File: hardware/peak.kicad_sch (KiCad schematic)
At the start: 29 parts, among them J1 Conn_Controller, J2 Conn_Buttons, J3 Conn_CAN, J4 Conn_Display, J5 Conn_DEBUG, Q1 AO3400A, U1 ESP32-S3-WROOM-1, U2 TLV76733DRVx, U3 MCP2542FDxMF

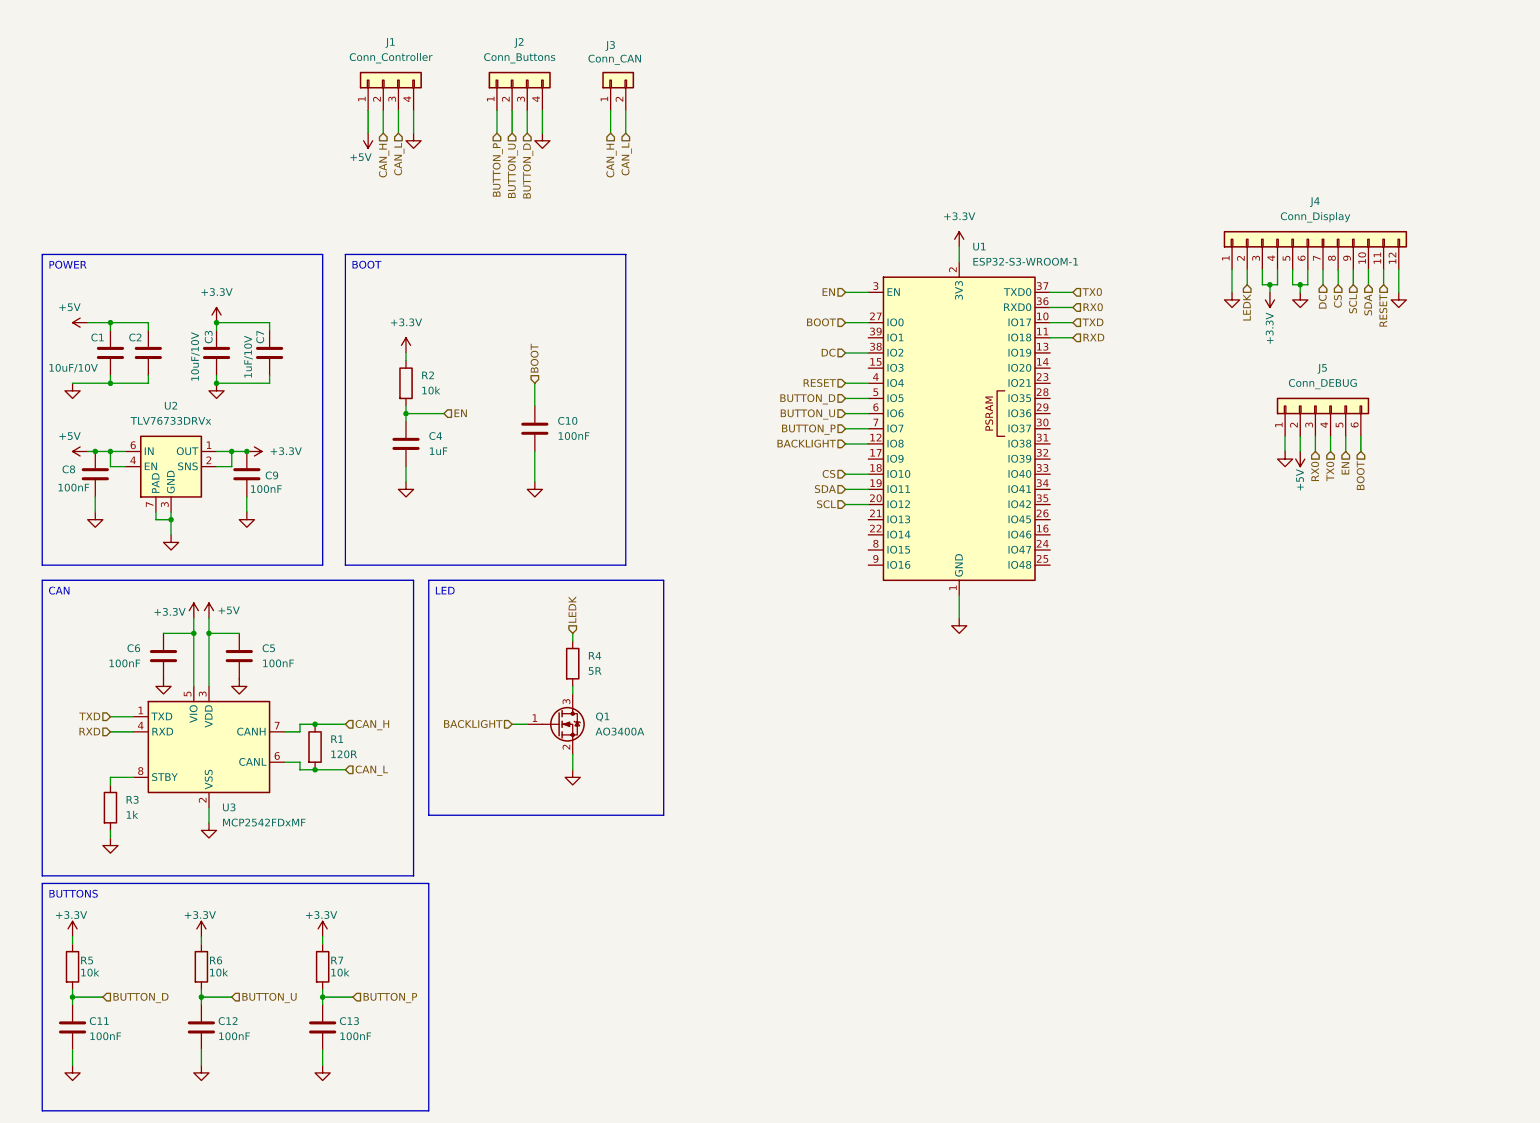
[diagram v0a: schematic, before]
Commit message: ✨ Add schematic parts
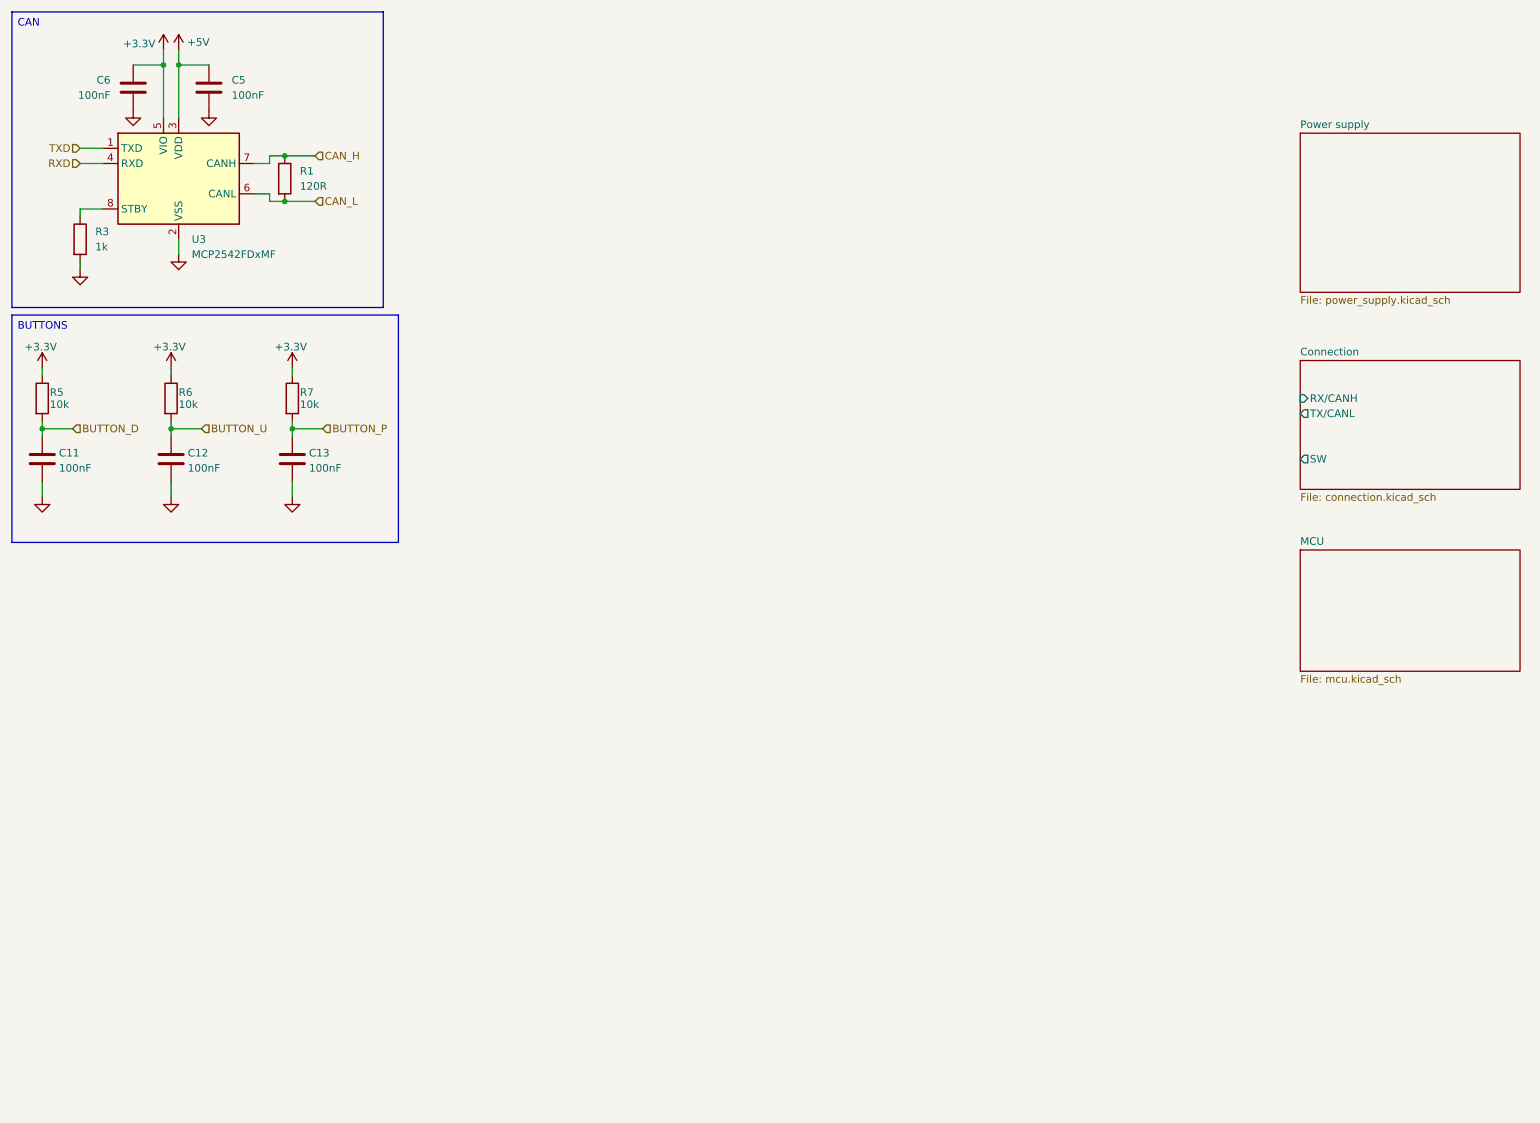
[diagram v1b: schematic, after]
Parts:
- removed C1, C2, C3: 10uF/10V, Capacitor_SMD:C_0805_2012Metric, symbol Device:C
- removed C10, C8, C9: 100nF, Capacitor_SMD:C_0603_1608Metric, symbol Device:C
- removed C4: 1uF, Capacitor_SMD:C_0603_1608Metric, symbol Device:C
- removed C7: 1uF/10V, Capacitor_SMD:C_0805_2012Metric, symbol Device:C
- removed J1: Conn_Controller, Connector_Molex:Molex_PicoBlade_53261-0471_1x04-1MP_P1.25mm_Horizontal, symbol Connector_Generic:Conn_01x04
- removed J2: Conn_Buttons, Connector_Molex:Molex_PicoBlade_53261-0471_1x04-1MP_P1.25mm_Horizontal, symbol Connector_Generic:Conn_01x04
- removed J3: Conn_CAN, Connector_Molex:Molex_PicoBlade_53261-0271_1x02-1MP_P1.25mm_Horizontal, symbol Connector_Generic:Conn_01x02
- removed J4: Conn_Display, lib:ST7789V2, symbol Connector_Generic:Conn_01x12
- removed J5: Conn_DEBUG, lib:DEBUG_SMD, symbol Connector_Generic:Conn_01x06
- removed Q1: AO3400A, PCM_Package_TO_SOT_SMD_AKL:SOT-23, symbol Transistor_FET:AO3400A
- removed R2: 10k, PCM_Resistor_SMD_AKL:R_0603_1608Metric, symbol Device:R
- removed R4: 5R, PCM_Resistor_SMD_AKL:R_0805_2012Metric, symbol Device:R
- removed U1: ESP32-S3-WROOM-1, RF_Module:ESP32-S3-WROOM-1, symbol RF_Module:ESP32-S3-WROOM-1
- removed U2: TLV76733DRVx, Package_SON:WSON-6-1EP_2x2mm_P0.65mm_EP1x1.6mm_ThermalVias, symbol Regulator_Linear:TLV76733DRVx
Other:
- added sheet Connection (connection.kicad_sch)
- added sheet MCU (mcu.kicad_sch)
- added sheet Power supply (power_supply.kicad_sch)
- moved on the sheet: C11, C12, C13, C5, C6, R1, R3, R5, R6, R7, U3

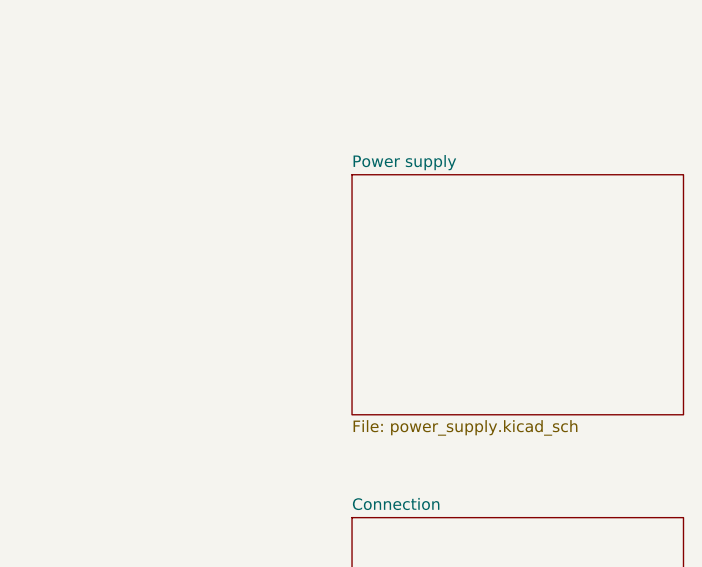
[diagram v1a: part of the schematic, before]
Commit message: ✨ Add pulldown to disable the led by default
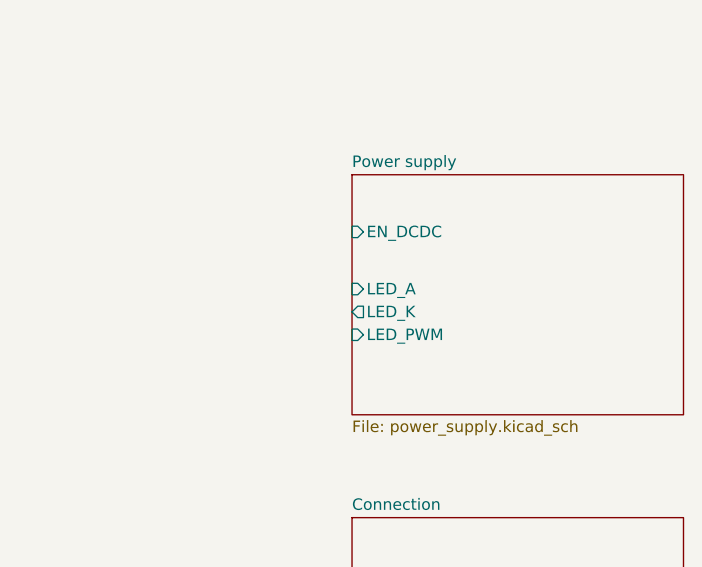
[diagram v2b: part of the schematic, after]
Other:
- sheet Power supply ports: added EN_DCDC, LED_A, LED_K, LED_PWM; removed none
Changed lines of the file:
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@@
+			)
+		)
+		(pin "EN_DCDC" input
+			(at 229.87 40.64 180)
+			(effects
+				(font
+					(size 1.27 1.27)
+				)
+				(justify left)
+			)
+		)
+		(pin "LED_A" input
+			(at 229.87 46.99 180)
+			(effects
+				(font
+					(size 1.27 1.27)
+				)
+				(justify left)
+			)
+		)
+		(pin "LED_K" output
+			(at 229.87 49.53 180)
+			(effects
+				(font
+					(size 1.27 1.27)
+				)
+				(justify left)
+			)
+		)
+		(pin "LED_PWM" input
+			(at 229.87 52.07 180)
+			(effects
+				(font
+					(size 1.27 1.27)
+				)
+				(justify left)
 			)
 		)

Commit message: ✨ Further schematic updates
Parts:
- removed C11, C12, C13, C5, C6: 100nF, Capacitor_SMD:C_0603_1608Metric, symbol Device:C
- removed R1: 120R, PCM_Resistor_SMD_AKL:R_0603_1608Metric, symbol Device:R
- removed R3: 1k, PCM_Resistor_SMD_AKL:R_0603_1608Metric, symbol Device:R
- removed R5, R6, R7: 10k, PCM_Resistor_SMD_AKL:R_0603_1608Metric, symbol Device:R
- removed U3: MCP2542FDxMF, Package_DFN_QFN:DFN-8-1EP_3x3mm_P0.65mm_EP1.55x2.4mm, symbol Interface_CAN_LIN:MCP2542FDxMF
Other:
- added sheet Display (display.kicad_sch)
- added sheet IO (io.kicad_sch)
- sheet MCU ports: added EN_DCDC, FB_DCDC; removed none
- sheet Power supply ports: added FB_DCDC; removed LED_A, LED_K, LED_PWM

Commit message: ✨ MCU updates
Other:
- added sheet Wireless (wireless.kicad_sch)
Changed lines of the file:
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@@
 	(wire
 		(pts
-			(xy 213.36 41.91) (xy 226.06 41.91)
+			(xy 173.99 59.69) (xy 226.06 59.69)
 		)
 		(stroke
@@
 	(wire
 		(pts
-			(xy 213.36 44.45) (xy 227.33 44.45)
+			(xy 173.99 62.23) (xy 227.33 62.23)
 		)
 		(stroke
@@
 	(wire
 		(pts
-			(xy 227.33 44.45) (xy 227.33 43.18)
-		)
-		(stroke
-			(width 0)
-			(type default)
-		)
-	)
-	(wire
-		(pts
-			(xy 226.06 41.91) (xy 226.06 40.64)
+			(xy 227.33 62.23) (xy 227.33 43.18)
+		)
+		(stroke
+			(width 0)
+			(type default)
+		)
+	)
+	(wire
+		(pts
+			(xy 226.06 59.69) (xy 226.06 40.64)
 		)
 		(stroke
@@
 	)
 	(sheet
-		(at 181.61 68.58)
+		(at 64.77 71.12)
 		(size 21.59 39.37)
 		(exclude_from_sim no)
@@
 		)
 		(property "Sheetname" "Display"
-			(at 181.61 67.8684 0)
+			(at 64.77 70.4084 0)
 			(effects
 				(font
@@
 		)
 		(property "Sheetfile" "display.kicad_sch"
-			(at 181.61 108.5346 0)
+			(at 64.77 111.0746 0)
 			(effects
 				(font
@@
 		)
 		(pin "DISPLAY_RESET" input
-			(at 203.2 74.93 0)
+			(at 86.36 77.47 0)
 			(effects
 				(font
@@
 		)
 		(pin "DISPLAY_TE" input
-			(at 203.2 77.47 0)
+			(at 86.36 80.01 0)
 			(effects
 				(font
@@
 		)
 		(pin "LED_PWM" input
-			(at 203.2 80.01 0)
+			(at 86.36 82.55 0)
 			(effects
 				(font
@@
 		)
 		(pin "MIPI_CLN" input
-			(at 203.2 82.55 0)
+			(at 86.36 85.09 0)
 			(effects
 				(font
@@
 		)
 		(pin "MIPI_CLP" input
-			(at 203.2 85.09 0)
+			(at 86.36 87.63 0)
 			(effects
 				(font
@@
 		)
 		(pin "MIPI_D0N" input
-			(at 203.2 87.63 0)
+			(at 86.36 90.17 0)
 			(effects
 				(font
@@
 		)
 		(pin "MIPI_D0P" input
-			(at 203.2 90.17 0)
+			(at 86.36 92.71 0)
 			(effects
 				(font
@@
 		)
 		(pin "MIPI_D1N" input
-			(at 203.2 92.71 0)
+			(at 86.36 95.25 0)
 			(effects
 				(font
@@
 		)
 		(pin "MIPI_D1P" input
-			(at 203.2 95.25 0)
+			(at 86.36 97.79 0)
 			(effects
 				(font
@@
 	)
 	(sheet
-		(at 176.53 36.83)
+		(at 125.73 104.14)
+		(size 33.02 31.75)
+		(exclude_from_sim no)
+		(in_bom yes)
+		(on_board yes)
+		(dnp no)
+		(fields_autoplaced yes)
+		(stroke
+			(width 0.1524)
+			(type solid)
+		)
+		(fill
+			(color 0 0 0 0.0000)
+		)
+		(property "Sheetname" "Wireless"
+			(at 125.73 103.4284 0)
+			(effects
+				(font
+					(size 1.27 1.27)
+				)
+				(justify left bottom)
+			)
+		)
+		(property "Sheetfile" "wireless.kicad_sch"
+			(at 125.73 136.4746 0)
+			(effects
+				(font
+					(size 1.27 1.27)
+				)
+				(justify left top)
+			)
+		)
+		(instances
+			(project "peak"
+				(path "/54a54a18-4a65-4728-b17a-32b4a97370c1"
+					(page "7")
+				)
+			)
+		)
+	)
+	(sheet
+		(at 137.16 54.61)
 		(size 36.83 20.32)
 		(exclude_from_sim no)
@@
 		)
 		(property "Sheetname" "MCU"
-			(at 176.53 36.1184 0)
+			(at 137.16 53.8984 0)
 			(effects
 				(font
@@
 		)
 		(property "Sheetfile" "mcu.kicad_sch"
-			(at 176.53 57.7346 0)
+			(at 137.16 75.5146 0)
 			(effects
 				(font
@@
 		)
 		(pin "EN_DCDC" input
-			(at 213.36 41.91 0)
+			(at 173.99 59.69 0)
 			(effects
 				(font
@@
 		)
 		(pin "FB_DCDC" input
-			(at 213.36 44.45 0)
-			(effects
-				(font
+			(at 173.99 62.23 0)
+			(effects
+				(font

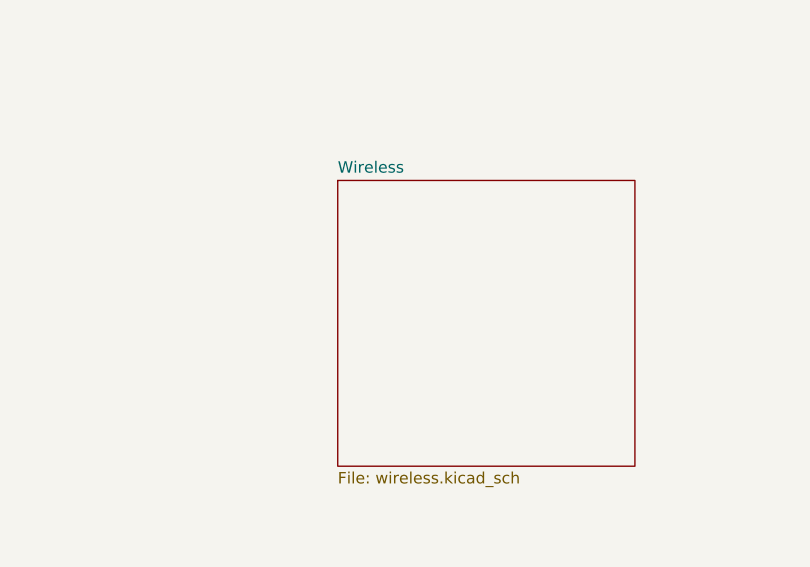
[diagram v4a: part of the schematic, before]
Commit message: ✨ Done wireless schematic
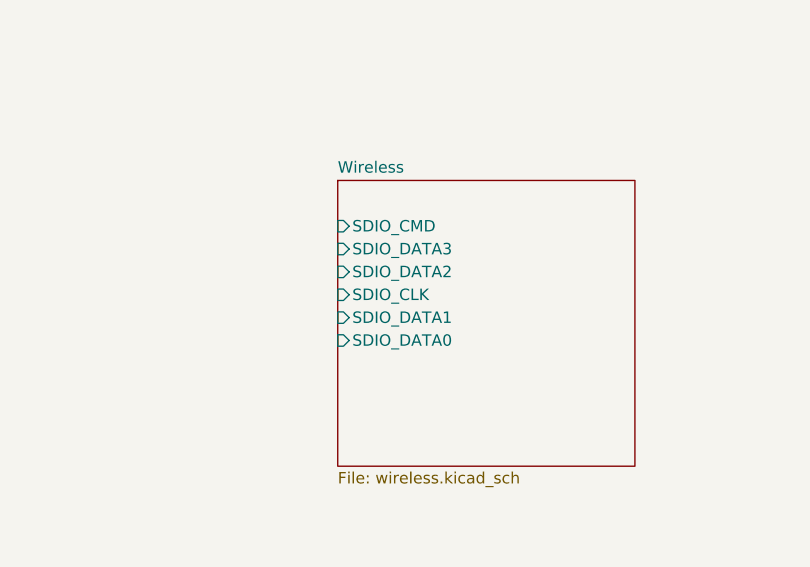
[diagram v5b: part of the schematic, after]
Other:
- sheet Wireless ports: added SDIO_CLK, SDIO_CMD, SDIO_DATA0, SDIO_DATA1, SDIO_DATA2, SDIO_DATA3; removed none
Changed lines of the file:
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@@
+			)
+		)
+		(pin "SDIO_CMD" input
+			(at 125.73 109.22 180)
+			(effects
+				(font
+					(size 1.27 1.27)
+				)
+				(justify left)
+			)
+		)
+		(pin "SDIO_DATA3" input
+			(at 125.73 111.76 180)
+			(effects
+				(font
+					(size 1.27 1.27)
+				)
+				(justify left)
+			)
+		)
+		(pin "SDIO_DATA2" input
+			(at 125.73 114.3 180)
+			(effects
+				(font
+					(size 1.27 1.27)
+				)
+				(justify left)
+			)
+		)
+		(pin "SDIO_CLK" input
+			(at 125.73 116.84 180)
+			(effects
+				(font
+					(size 1.27 1.27)
+				)
+				(justify left)
+			)
+		)
+		(pin "SDIO_DATA1" input
+			(at 125.73 119.38 180)
+			(effects
+				(font
+					(size 1.27 1.27)
+				)
+				(justify left)
+			)
+		)
+		(pin "SDIO_DATA0" input
+			(at 125.73 121.92 180)
+			(effects
+				(font
+					(size 1.27 1.27)
+				)
+				(justify left)
 			)
 		)

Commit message: 📂 PCB updates
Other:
- sheet Connection ports: added Button_D, Button_P, Button_U, CANH, CANL, RX, TX; removed RX/CANH, TX/CANL
- sheet MCU ports: added BUTTON_D, BUTTON_P, BUTTON_U, DISPLAY_RESET, DISPLAY_TE, LED_PWM, MIPI_CLN, MIPI_CLP, MIPI_D0N, MIPI_D0P, MIPI_D1N, MIPI_D1P, RX_CAN, RX_MCU, SCL_MCU, SDA_MCU, SDIO_CLK, SDIO_CMD, SDIO_DATA0, SDIO_DATA1, SDIO_DATA2, SDIO_DATA3, SW_MCU, TX_CAN, TX_MCU, VBUS_MCU; removed none

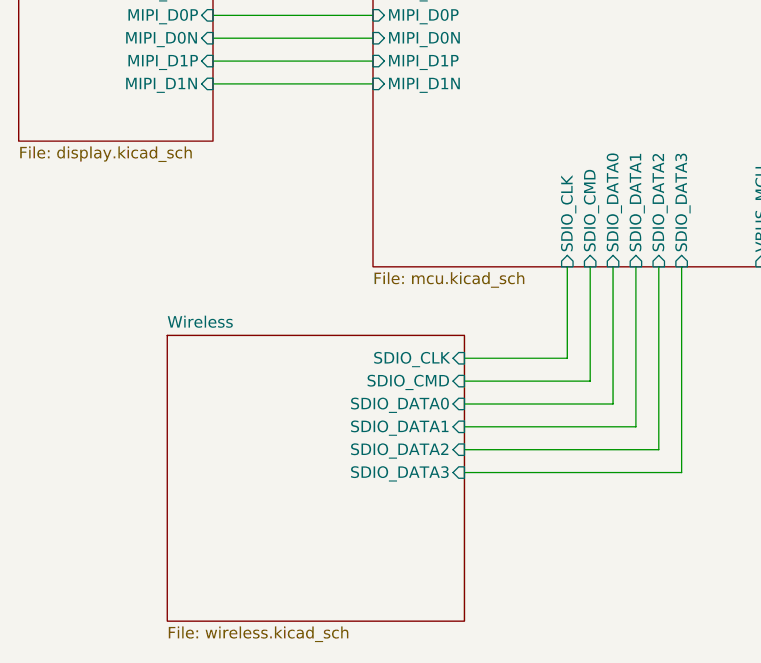
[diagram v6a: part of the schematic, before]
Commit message: 🐛 Fix errors from rev1.0
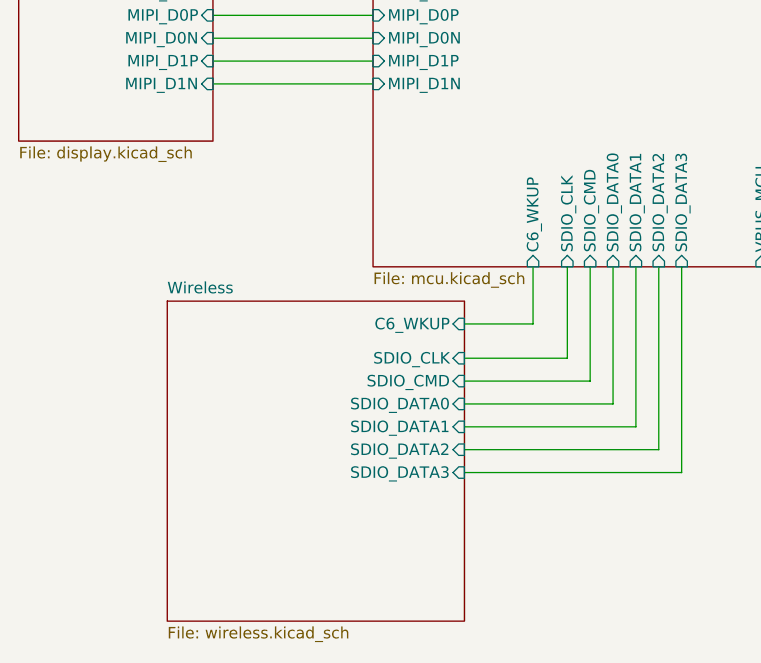
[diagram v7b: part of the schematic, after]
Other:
- sheet MCU ports: added C6_WKUP; removed none
- sheet Wireless ports: added C6_WKUP; removed none
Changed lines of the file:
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@@
+	(wire
+		(pts
+			(xy 130.81 127) (xy 138.43 127)
+		)
+		(stroke
+			(width 0)
+			(type default)
+		)
+	)
 	(wire
 		(pts
@@
 		(pts
 			(xy 130.81 133.35) (xy 144.78 133.35)
+		)
+		(stroke
+			(width 0)
+			(type default)
+		)
+	)
+	(wire
+		(pts
+			(xy 138.43 127) (xy 138.43 120.65)
 		)
 		(stroke
@@
 	)
 	(sheet
-		(at 97.79 128.27)
-		(size 33.02 31.75)
+		(at 97.79 124.46)
+		(size 33.02 35.56)
 		(exclude_from_sim no)
 		(in_bom yes)
@@
 		)
 		(property "Sheetname" "Wireless"
-			(at 97.79 127.5584 0)
+			(at 97.79 123.7484 0)
 			(effects
 				(font
@@
 		(pin "SDIO_DATA0" input
 			(at 130.81 135.89 0)
+			(effects
+				(font
+					(size 1.27 1.27)
+				)
+				(justify right)
+			)
+		)
+		(pin "C6_WKUP" input
+			(at 130.81 127 0)
 			(effects
 				(font
@@
 			(effects
 				(font
+					(size 1.27 1.27)
+				)
+				(justify left)
+			)
+		)
+		(pin "C6_WKUP" input
+			(at 138.43 120.65 270)
+			(effects
+				(font
